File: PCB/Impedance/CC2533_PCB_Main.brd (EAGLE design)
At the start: 69.5 x 40.3 mm, 44 parts

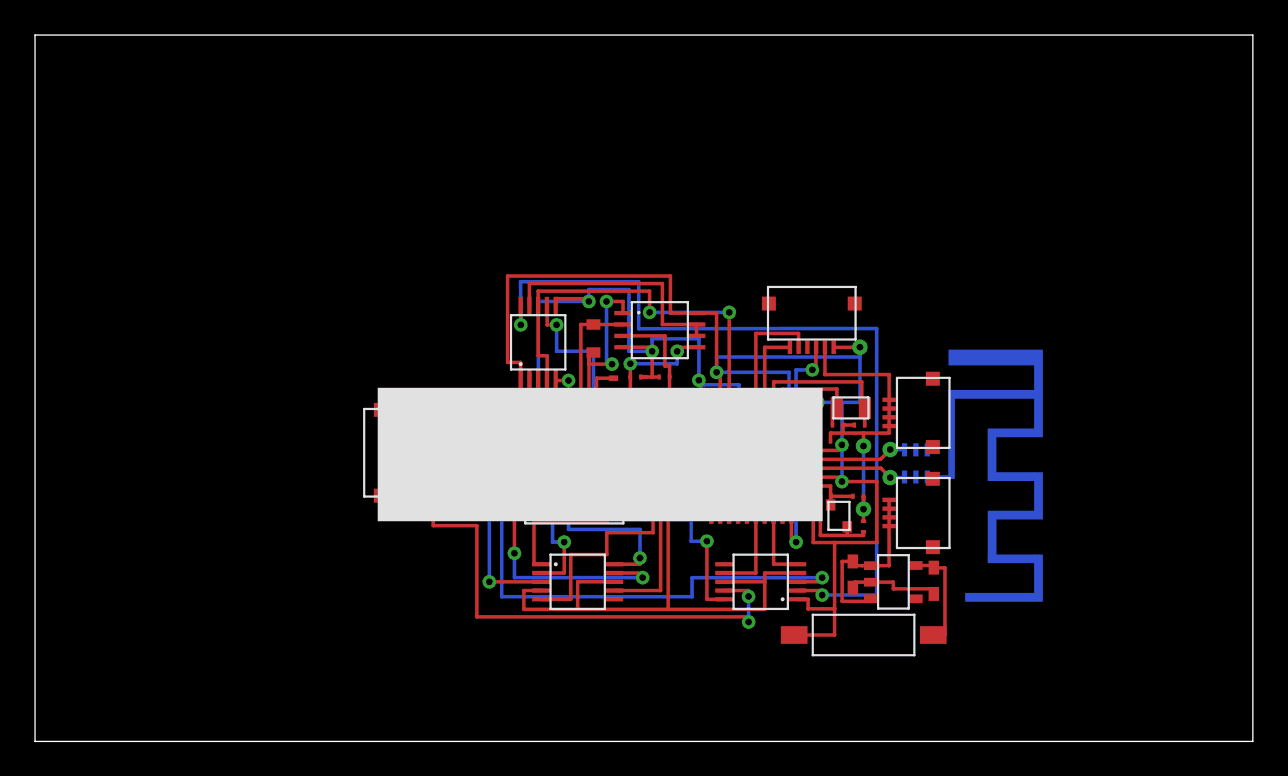
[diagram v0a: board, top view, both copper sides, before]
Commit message: New updates
Added new layout of CC2533 voltage stim and AD5933 impeance analysis
with ground planes (completed), and that of AD5933 impedance analysis
only.
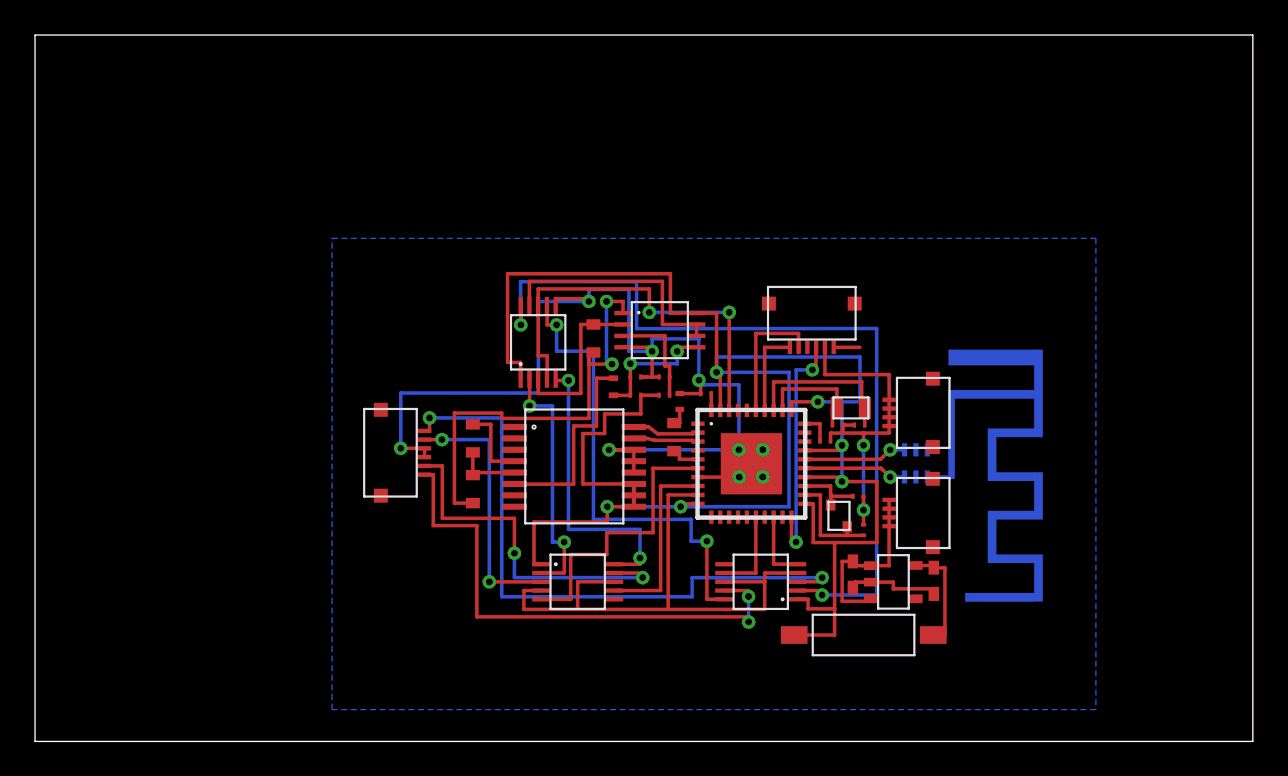
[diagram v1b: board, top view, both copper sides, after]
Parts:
- removed U$32, U$33, U$36, U$42, U$43, U$44, U$45, U$46, U$47, U$48: DRILL_HOLE, CC2530_PCB_TL:DRILL_HOLE
- moved U$4 0.20 mm to (47.3, 12.1)
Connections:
- net GND: no longer U$42.1, U$43.1, U$44.1, U$45.1, U$46.1, U$47.1
- net N$1: no longer U$32.1
- net N$2: no longer U$33.1
- net VDD: no longer U$36.1, U$48.1
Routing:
- net VDD: track 122.1 -> 124.3 mm, vias 5 -> 6
- net GND: track 95.4 -> 94.2 mm, vias 5 -> 11
- net N$2: track 5.95 -> 5.93 mm, vias 0 -> 1
- net N$1: track 5.95 -> 5.93 mm, vias 0 -> 1
- added copper zone on layer 16, net N$26
